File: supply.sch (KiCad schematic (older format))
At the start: 65 parts, among them IC1 TPS54561, J10 61300311121, J3 DC_SOCKET, U4 TPS65296, U5 TPS62823DLCT

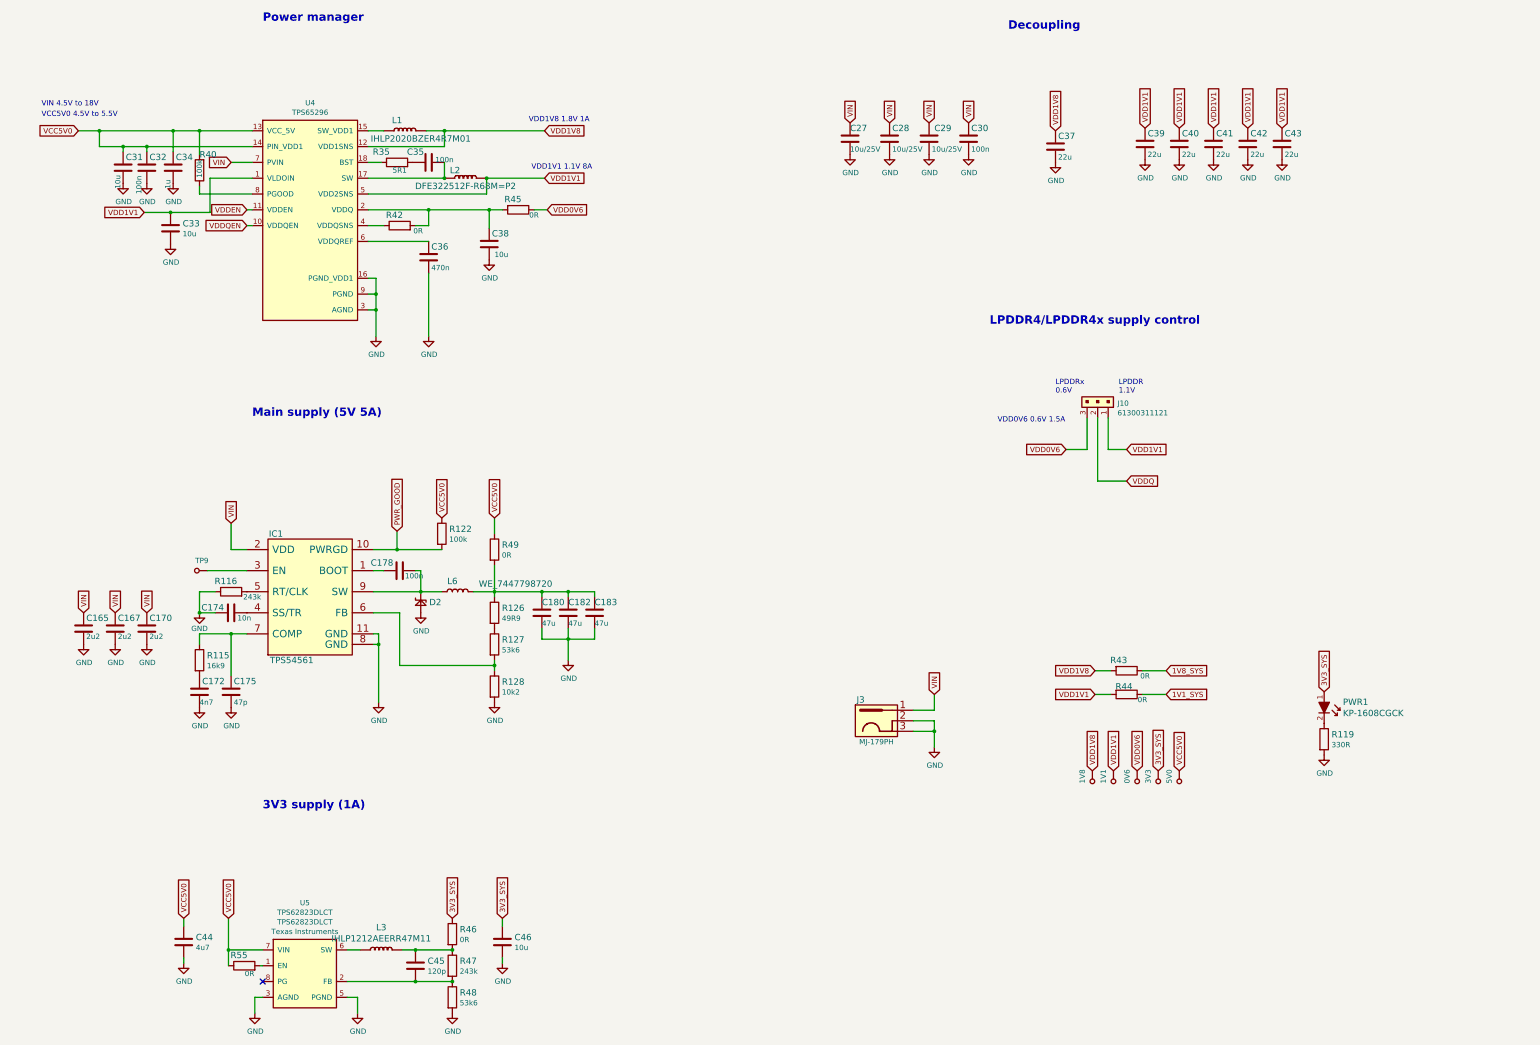
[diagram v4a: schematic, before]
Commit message: Make Supply more compact
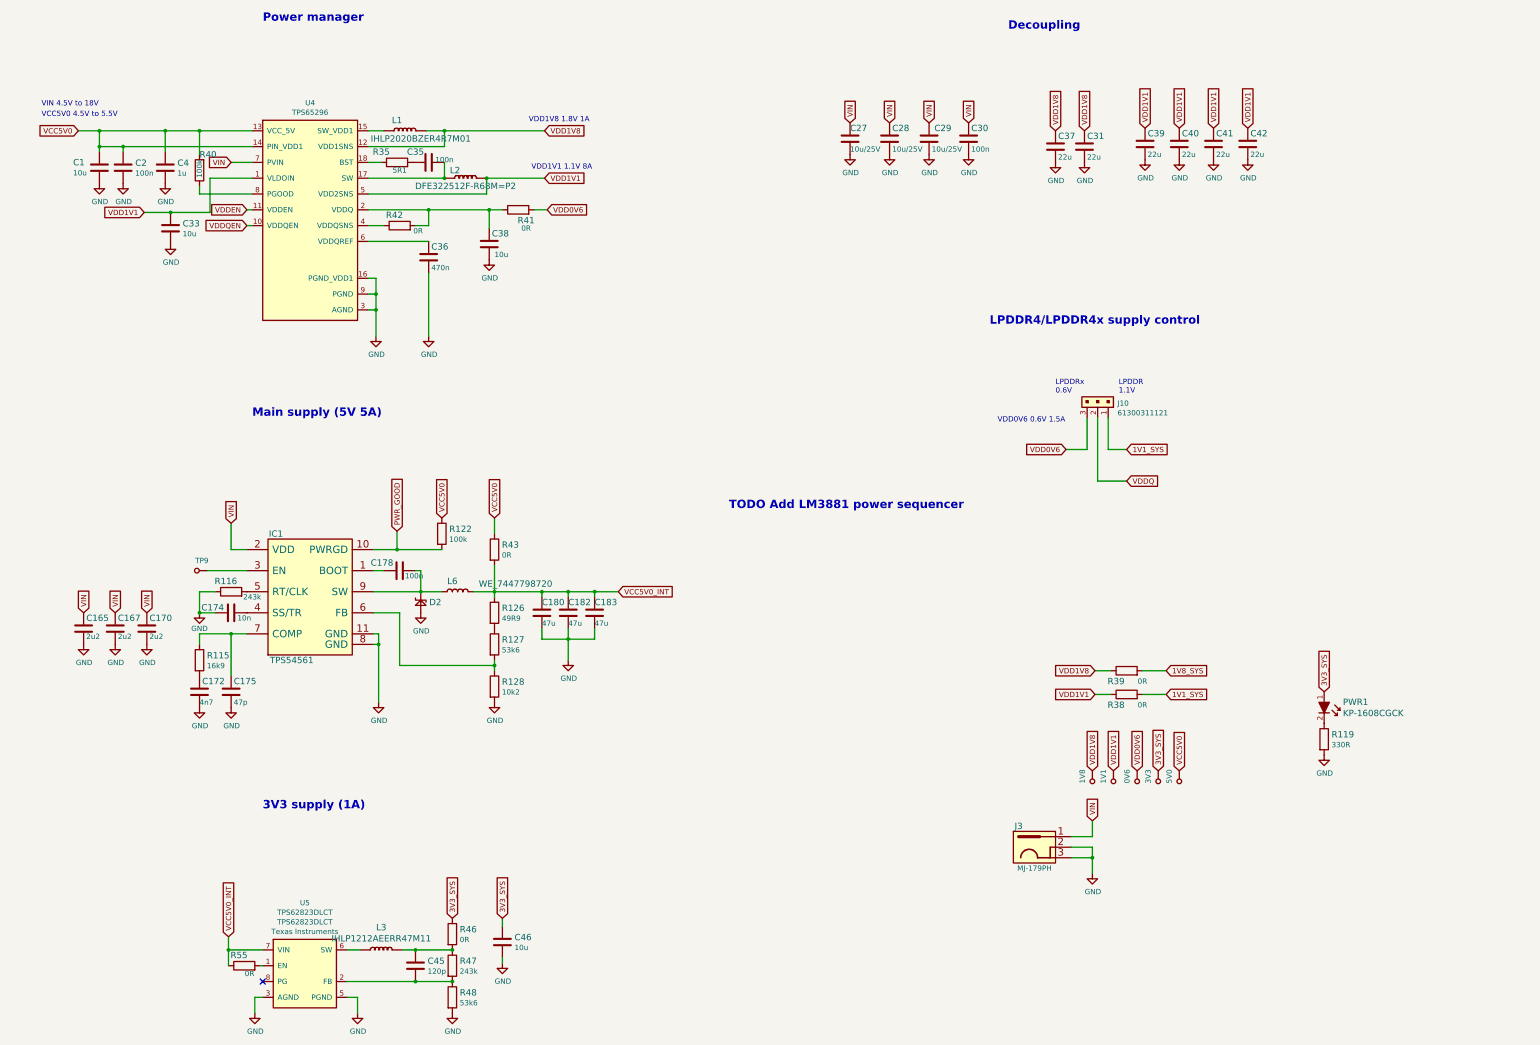
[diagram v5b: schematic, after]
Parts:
- removed C31: C_10u_0402, lpddr4-test-board-footprints:0402-cap, symbol lpddr4-test-board:C_10u_0402
- removed C32: C_100n_0402_6V3, lpddr4-test-board-footprints:0402-cap, symbol lpddr4-test-board:C_100n_0402_6V3
- removed C34: C_1u_0402, lpddr4-test-board-footprints:0402-cap, symbol lpddr4-test-board:C_1u_0402
- removed C43: C_22u_0603, lpddr4-test-board-footprints:0603-cap, symbol lpddr4-test-board:C_22u_0603
- removed C44: C_4u7_0603, antmicro-footprints:0603-cap, symbol antmicroCapacitors0603:C_4u7_0603
- removed R43, R44, R45, R49: R_0R_1206, lpddr4-test-board-footprints:1206-res, symbol lpddr4-test-board:R_0R_1206
- added C1: C_10u_0603, lpddr4-test-board-footprints:0603-cap, symbol lpddr4-test-board:C_10u_0603
- added C2: C_100n_0603, antmicro-footprints:0603-cap, symbol antmicroCapacitors0603:C_100n_0603
- added C31: C_22u_0603, lpddr4-test-board-footprints:0603-cap, symbol lpddr4-test-board:C_22u_0603
- added C4: C_1u_0603, antmicro-footprints:0603-cap, symbol antmicroCapacitors0603:C_1u_0603
- added R38, R39, R41, R43: R_0R_0603, antmicro-footprints:0603-res, symbol antmicroResistors0603:R_0R_0603
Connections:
- net 1V1_SYS: now also J10.1, R38.2
- net 1V8_SYS: now also R39.2
- net GND: now also C1.2, C2.2, C31.2, C4.2
- net VCC5V0: now also C1.1, C2.1, C4.1, R43.1; no longer R55.1, U5.7 (VIN)
- net VDD0V6: now also R41.2
- net VDD1V1: now also R38.1; no longer J10.1
- net VDD1V8: now also C31.1, R39.1
- net at C38.1, R42.2, U4.2 (VDDQ): now also R41.1
- net VCC5V0_INT: now reaches C180.1, C182.1, C183.1, L6.2 (P), R126.1
- net VCC5V0_INT: now also R55.1, U5.7 (VIN), R43.2
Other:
- note added: "TODO Add LM3881 power sequencer"
- moved on the sheet: J3

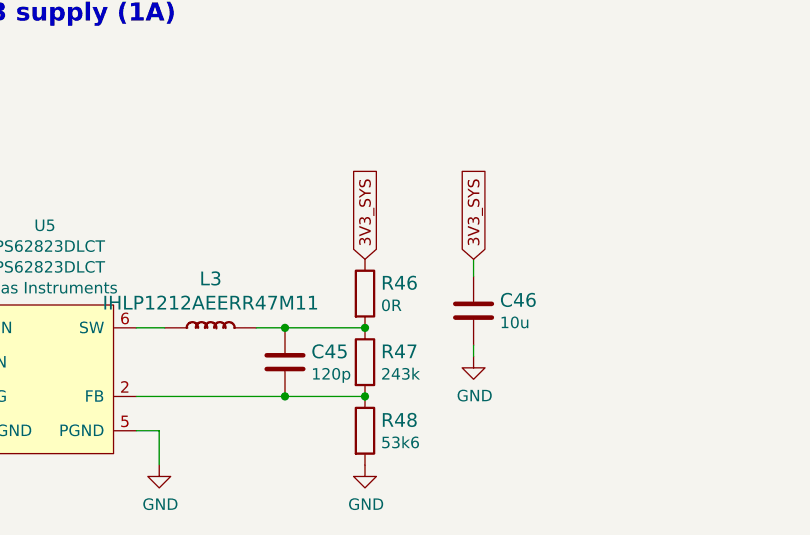
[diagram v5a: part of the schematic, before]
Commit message: Signal routing ready - DRC clean
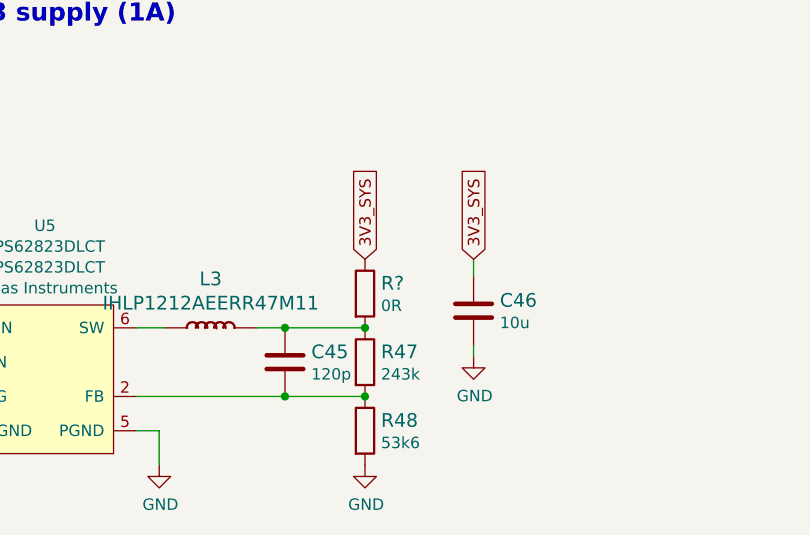
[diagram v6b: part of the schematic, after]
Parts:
- removed R46: R_0R_1206, lpddr4-test-board-footprints:1206-res, symbol lpddr4-test-board:R_0R_1206
- added R?: R_0R_0603, antmicro-footprints:0603-res, symbol antmicroResistors0603:R_0R_0603
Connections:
- net 3V3_SYS: now also R?.1
- net at C45.1, L3.2 (P), R47.1: now also R?.2
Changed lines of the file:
@@
 	0    1    1    0
 $EndComp
-Connection ~ 5350 9775
 $Comp
 L lpddr4-test-board:R_243k_0402 R47
@@
 Wire Wire Line
 	5000 10075 5350 10075
-$Comp
-L lpddr4-test-board:R_0R_1206 R46
-U 1 1 6021B240
-P 5350 9625
-F 0 "R46" V 5305 9695 60  0000 L CNN
-F 1 "R_0R_1206" H 5350 9475 60  0001 C CNN
-F 2 "lpddr4-test-board-footprints:1206-res" H 5550 9825 60  0001 L CNN
-F 3 "" H 5350 9625 50  0001 C CNN
-F 4 "MULTICOMP" H 5550 10025 60  0001 L CNN "Manufacturer"
-F 5 "MCMR12X000_PTL" H 5550 9925 60  0001 L CNN "MPN"
-F 6 "0R" V 5403 9695 50  0000 L CNN "Val"
-	1    5350 9625
-	0    1    1    0
-$EndComp
 Text Notes 10625 1050 0    79   ~ 16
 Decoupling
@@
 Text GLabel 3225 9650 1    50   Input ~ 0
 VCC5V0_INT
+$Comp
+L antmicroResistors0603:R_0R_0603 R?
+U 1 1 5FD15A52
+P 5350 9625
+F 0 "R?" V 5305 9695 60  0000 L CNN
+F 1 "R_0R_0603" H 5350 9475 60  0001 C CNN
+F 2 "antmicro-footprints:0603-res" H 5550 9825 60  0001 L CNN
+F 3 "" H 5350 9625 50  0001 C CNN
+F 4 "BOURNS" H 5550 10025 60  0001 L CNN "Manufacturer"
+F 5 "CR0603-J/-000ELF" H 5550 9925 60  0001 L CNN "MPN"
+F 6 "0R" V 5403 9695 50  0000 L CNN "Val"
+	1    5350 9625
+	0    1    1    0
+$EndComp
+Connection ~ 5350 9775
 $EndSCHEMATC

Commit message: Minor change
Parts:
- gave numbers to parts that had none: 1
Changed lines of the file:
@@
 VCC5V0_INT
 $Comp
-L antmicroResistors0603:R_0R_0603 R?
+L antmicroResistors0603:R_0R_0603 R44
 U 1 1 5FD15A52
 P 5350 9625
-F 0 "R?" V 5305 9695 60  0000 L CNN
+F 0 "R44" V 5305 9695 60  0000 L CNN
 F 1 "R_0R_0603" H 5350 9475 60  0001 C CNN
 F 2 "antmicro-footprints:0603-res" H 5550 9825 60  0001 L CNN

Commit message: Update component library
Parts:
- C2: footprint antmicro-footprints:0603-cap -> lpddr4-test-board-footprints:0603-cap; symbol antmicroCapacitors0603:C_100n_0603 -> lpddr4-test-board:C_100n_0603
- C4: footprint antmicro-footprints:0603-cap -> lpddr4-test-board-footprints:0603-cap; symbol antmicroCapacitors0603:C_1u_0603 -> lpddr4-test-board:C_1u_0603
- C45: footprint antmicro-footprints:0603-cap -> lpddr4-test-board-footprints:0603-cap; symbol antmicroCapacitors0603:C_120p_0603 -> lpddr4-test-board:C_120p_0603
- J10: footprint antmicro-footprints:PinHeader_1x3_P2.54_Drill1.1mm -> lpddr4-test-board-footprints:PinHeader_1x3_P2.54_Drill1.1mm; symbol antmicroRectangularConnectorsHeadersMalePins:61300311121 -> lpddr4-test-board:61300311121
- R35: footprint antmicro-footprints:0402-res -> lpddr4-test-board-footprints:0402-res; symbol antmicroResistors0402:R_5R1_0402 -> lpddr4-test-board:R_5R1_0402
- R38, R39, R41, R43, R44: footprint antmicro-footprints:0603-res -> lpddr4-test-board-footprints:0603-res; symbol antmicroResistors0603:R_0R_0603 -> lpddr4-test-board:R_0R_0603
- R55: footprint antmicro-footprints:0402-res -> lpddr4-test-board-footprints:0402-res; symbol antmicroResistors0402:R_0R_0402 -> lpddr4-test-board:R_0R_0402
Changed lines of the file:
@@
 $EndComp
 $Comp
-L antmicroRectangularConnectorsHeadersMalePins:61300311121 J10
+L lpddr4-test-board:61300311121 J10
 U 1 1 603FC14E
 P 11575 4575
 F 0 "J10" H 11487 4587 50  0000 R CNN
 F 1 "61300311121" H 11487 4678 50  0000 R CNN
-F 2 "antmicro-footprints:PinHeader_1x3_P2.54_Drill1.1mm" H 11775 4775 60  0001 L CNN
+F 2 "lpddr4-test-board-footprints:PinHeader_1x3_P2.54_Drill1.1mm" H 11775 4775 60  0001 L CNN
 F 3 "https://katalog.we-online.de/em/datasheet/6130xx11121.pdf" H 11775 4875 60  0001 L CNN
 F 4 "61300311121" H 11775 5075 60  0001 L CNN "MPN"
@@
 	5700 2750 5825 2750
 $Comp
-L antmicroResistors0402:R_0R_0402 R55
+L lpddr4-test-board:R_0R_0402 R55
 U 1 1 60B2C496
 P 3375 9925
 F 0 "R55" H 3325 10025 60  0000 C CNN
 F 1 "R_0R_0402" H 3375 9775 60  0001 C CNN
-F 2 "antmicro-footprints:0402-res" H 3575 10125 60  0001 L CNN
+F 2 "lpddr4-test-board-footprints:0402-res" H 3575 10125 60  0001 L CNN
 F 3 "" H 3375 9925 50  0001 C CNN
 F 4 "PANASONIC" H 3575 10325 60  0001 L CNN "Manufacturer"
@@
 $EndComp
 $Comp
-L antmicroCapacitors0603:C_120p_0603 C45
+L lpddr4-test-board:C_120p_0603 C45
 U 1 1 60B43827
 P 5000 9925
 F 0 "C45" H 5115 9970 60  0000 L CNN
 F 1 "C_120p_0603" H 5000 9775 60  0001 C CNN
-F 2 "antmicro-footprints:0603-cap" H 5200 10125 60  0001 L CNN
+F 2 "lpddr4-test-board-footprints:0603-cap" H 5200 10125 60  0001 L CNN
 F 3 "" H 5000 9925 50  0001 C CNN
 F 4 "WALSIN" H 5200 10325 60  0001 L CNN "Manufacturer"
@@
 Decoupling
 $Comp
-L antmicroResistors0402:R_5R1_0402 R35
+L lpddr4-test-board:R_5R1_0402 R35
 U 1 1 604E9209
 P 4825 2300
 F 0 "R35" H 4675 2400 60  0000 C CNN
 F 1 "R_5R1_0402" H 4825 2150 60  0001 C CNN
-F 2 "antmicro-footprints:0402-res" H 5025 2500 60  0001 L CNN
+F 2 "lpddr4-test-board-footprints:0402-res" H 5025 2500 60  0001 L CNN
 F 3 "" H 4825 2300 50  0001 C CNN
 F 4 "PANASONIC" H 5025 2700 60  0001 L CNN "Manufacturer"
@@
 TODO Add LM3881 power sequencer
 $Comp
-L antmicroCapacitors0603:C_1u_0603 C4
+L lpddr4-test-board:C_1u_0603 C4
 U 1 1 5FCD598A
 P 2625 2350
 F 0 "C4" H 2740 2395 60  0000 L CNN
 F 1 "C_1u_0603" H 2625 2200 60  0001 C CNN
-F 2 "antmicro-footprints:0603-cap" H 2825 2550 60  0001 L CNN
+F 2 "lpddr4-test-board-footprints:0603-cap" H 2825 2550 60  0001 L CNN
 F 3 "" H 2625 2350 50  0001 C CNN
 F 4 "WALSIN" H 2825 2750 60  0001 L CNN "Manufacturer"
@@
 $EndComp
 $Comp
-L antmicroCapacitors0603:C_100n_0603 C2
+L lpddr4-test-board:C_100n_0603 C2
 U 1 1 5FCD7977
 P 2225 2350
 F 0 "C2" H 2340 2395 60  0000 L CNN
 F 1 "C_100n_0603" H 2225 2200 60  0001 C CNN
-F 2 "antmicro-footprints:0603-cap" H 2425 2550 60  0001 L CNN
+F 2 "lpddr4-test-board-footprints:0603-cap" H 2425 2550 60  0001 L CNN
 F 3 "" H 2225 2350 50  0001 C CNN
 F 4 "AVX" H 2425 2750 60  0001 L CNN "Manufacturer"
@@
 $EndComp
 $Comp
-L antmicroResistors0603:R_0R_0603 R38
+L lpddr4-test-board:R_0R_0603 R38
 U 1 1 5FD73258
 P 11750 7350
 F 0 "R38" H 11650 7250 60  0000 C CNN
 F 1 "R_0R_0603" H 11750 7200 60  0001 C CNN
-F 2 "antmicro-footprints:0603-res" H 11950 7550 60  0001 L CNN
+F 2 "lpddr4-test-board-footprints:0603-res" H 11950 7550 60  0001 L CNN
 F 3 "" H 11750 7350 50  0001 C CNN
 F 4 "BOURNS" H 11950 7750 60  0001 L CNN "Manufacturer"
@@
 $EndComp
 $Comp
-L antmicroResistors0603:R_0R_0603 R39
+L lpddr4-test-board:R_0R_0603 R39
 U 1 1 5FDA5C63
 P 11750 7125
 F 0 "R39" H 11650 7025 60  0000 C CNN
 F 1 "R_0R_0603" H 11750 6975 60  0001 C CNN
-F 2 "antmicro-footprints:0603-res" H 11950 7325 60  0001 L CNN
+F 2 "lpddr4-test-board-footprints:0603-res" H 11950 7325 60  0001 L CNN
 F 3 "" H 11750 7125 50  0001 C CNN
 F 4 "BOURNS" H 11950 7525 60  0001 L CNN "Manufacturer"
@@
 $EndComp
 $Comp
-L antmicroResistors0603:R_0R_0603 R41
+L lpddr4-test-board:R_0R_0603 R41
 U 1 1 5FDAEBDB
 P 5975 2750
 F 0 "R41" H 6050 2650 60  0000 C CNN
 F 1 "R_0R_0603" H 5975 2600 60  0001 C CNN
-F 2 "antmicro-footprints:0603-res" H 6175 2950 60  0001 L CNN
+F 2 "lpddr4-test-board-footprints:0603-res" H 6175 2950 60  0001 L CNN
 F 3 "" H 5975 2750 50  0001 C CNN
 F 4 "BOURNS" H 6175 3150 60  0001 L CNN "Manufacturer"
@@
 $EndComp
 $Comp
-L antmicroResistors0603:R_0R_0603 R43
+L lpddr4-test-board:R_0R_0603 R43
 U 1 1 5FDBEC32
 P 5750 5975
 F 0 "R43" V 5705 6045 60  0000 L CNN
 F 1 "R_0R_0603" H 5750 5825 60  0001 C CNN
-F 2 "antmicro-footprints:0603-res" H 5950 6175 60  0001 L CNN
+F 2 "lpddr4-test-board-footprints:0603-res" H 5950 6175 60  0001 L CNN
 F 3 "" H 5750 5975 50  0001 C CNN
 F 4 "BOURNS" H 5950 6375 60  0001 L CNN "Manufacturer"
@@
 VCC5V0_INT
 $Comp
-L antmicroResistors0603:R_0R_0603 R44
+L lpddr4-test-board:R_0R_0603 R44
 U 1 1 5FD15A52
 P 5350 9625
 F 0 "R44" V 5305 9695 60  0000 L CNN
 F 1 "R_0R_0603" H 5350 9475 60  0001 C CNN
-F 2 "antmicro-footprints:0603-res" H 5550 9825 60  0001 L CNN
+F 2 "lpddr4-test-board-footprints:0603-res" H 5550 9825 60  0001 L CNN
 F 3 "" H 5350 9625 50  0001 C CNN
 F 4 "BOURNS" H 5550 10025 60  0001 L CNN "Manufacturer"
